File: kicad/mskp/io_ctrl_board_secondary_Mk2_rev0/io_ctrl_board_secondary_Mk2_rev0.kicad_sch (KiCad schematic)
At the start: 25 parts, among them J1 USB_C_I2C_input, J2 Keypad_matrix_connector_JST, J3 OLED_128x64, J4 I2C_aux_JST, J5 RJ45_SPI_I2C_input, J6 SPI_aux_JST, J7 I2C_aux_pads, U1 MCP23017_SP, U2 AMS1117

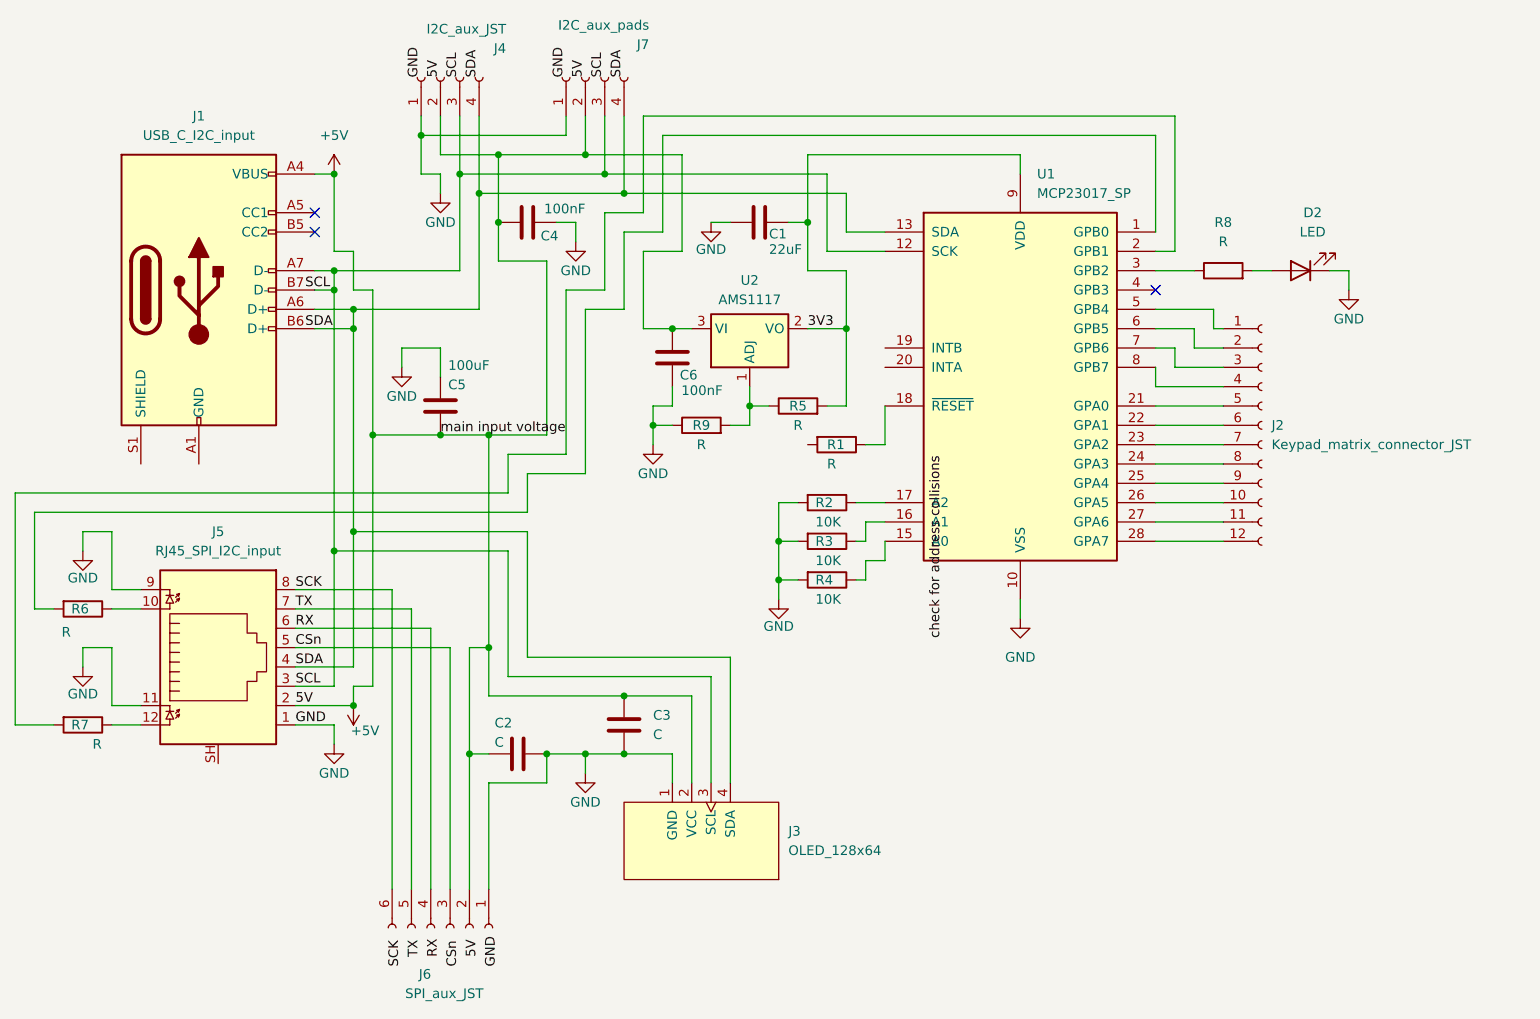
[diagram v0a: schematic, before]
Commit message: Further refinement of first drafts adding specific components
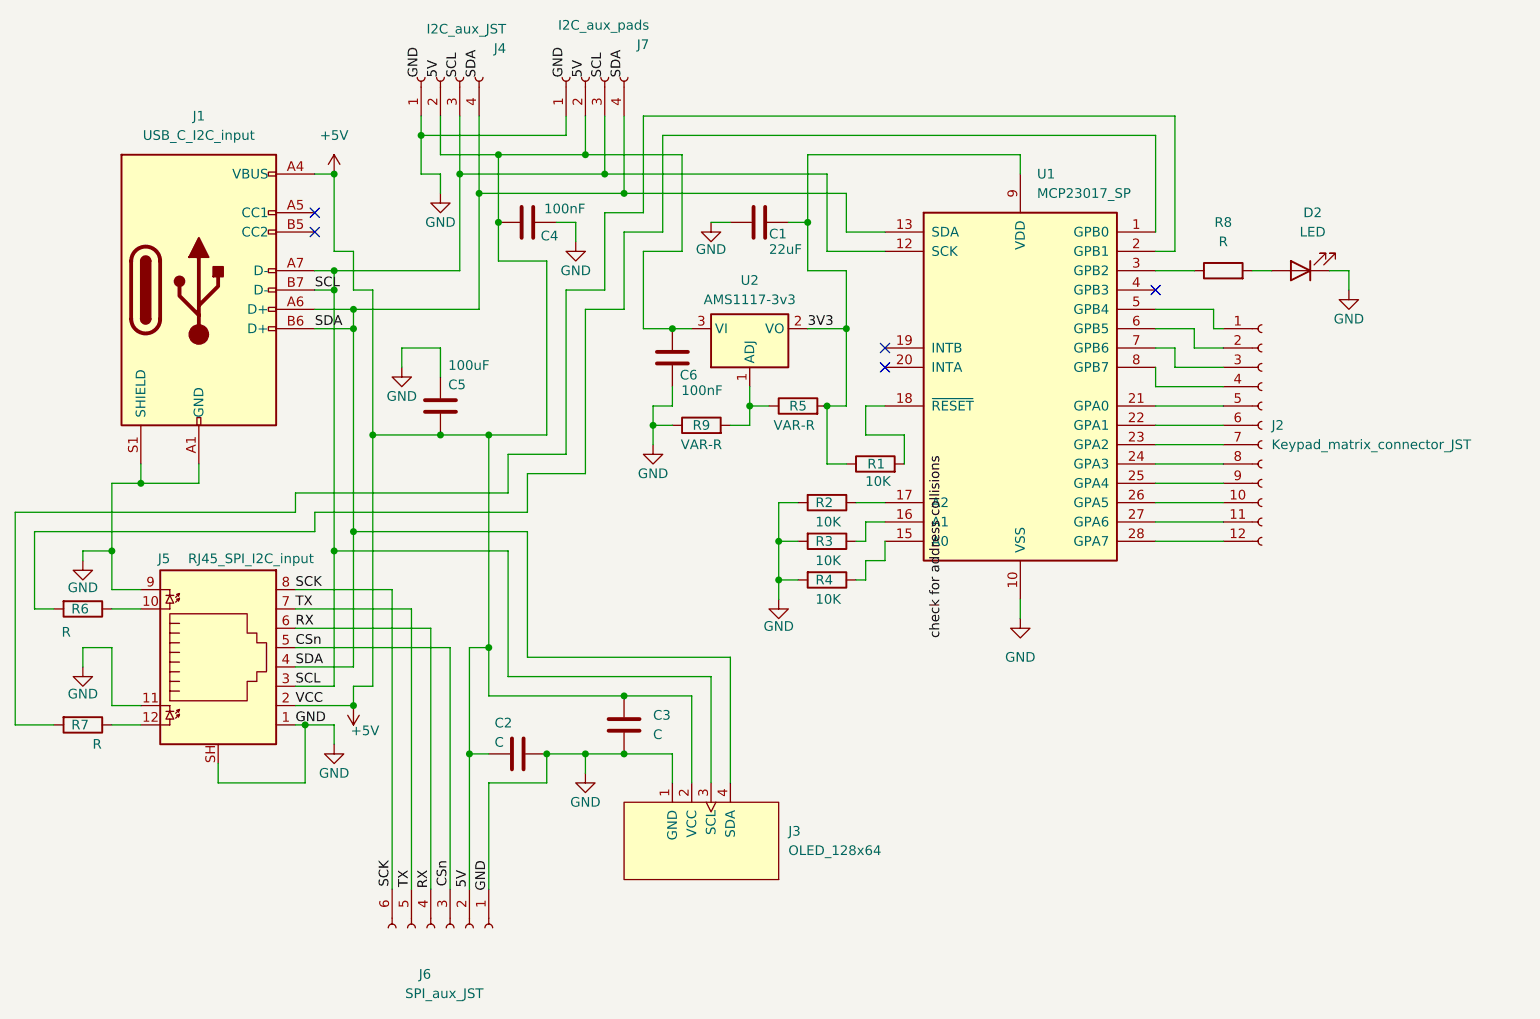
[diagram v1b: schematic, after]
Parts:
- R1: value R -> 10K
- R5, R9: value R -> VAR-R
- U2: value AMS1117 -> AMS1117-3v3
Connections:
- net 3V3: now also R1.1
- net GND: now also J1.A1 (GND), J1.A12 (GND), J1.B1 (GND), J1.B12 (GND), J1.S1 (SHIELD), J5.SH
- net at U1.18 (~{RESET}): now also R1.2; no longer R1.1
- no-connect marks 3 -> 5
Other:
- moved on the sheet: R1

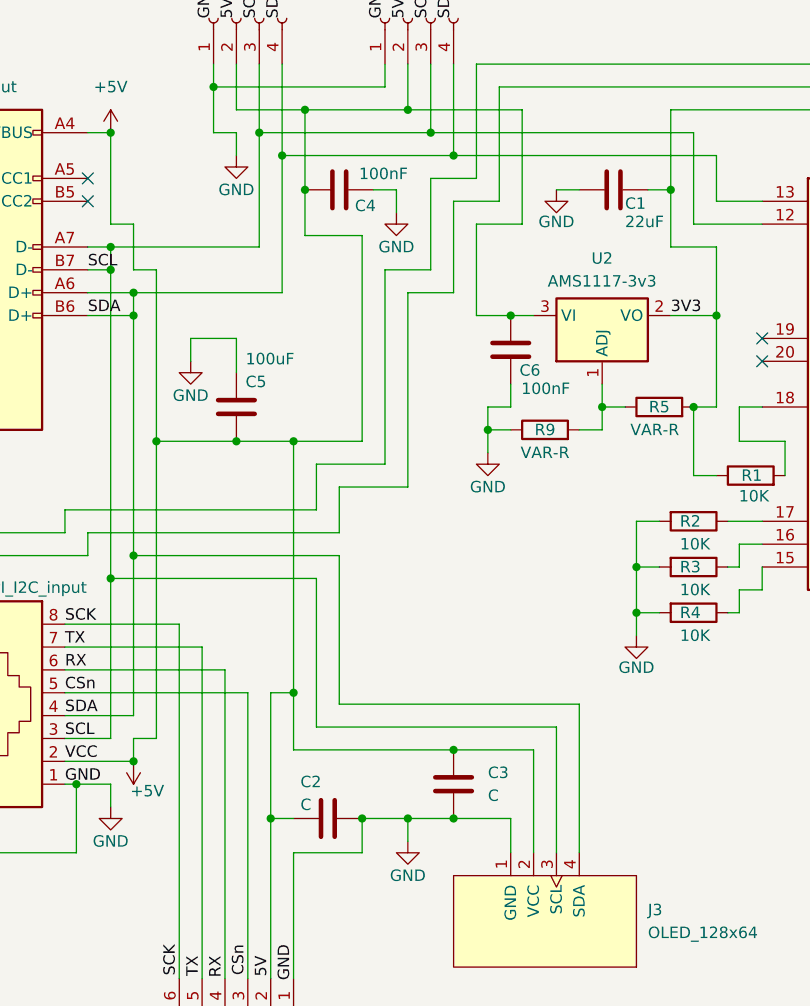
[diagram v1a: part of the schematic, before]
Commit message: Initital footprint assignment to all control boards
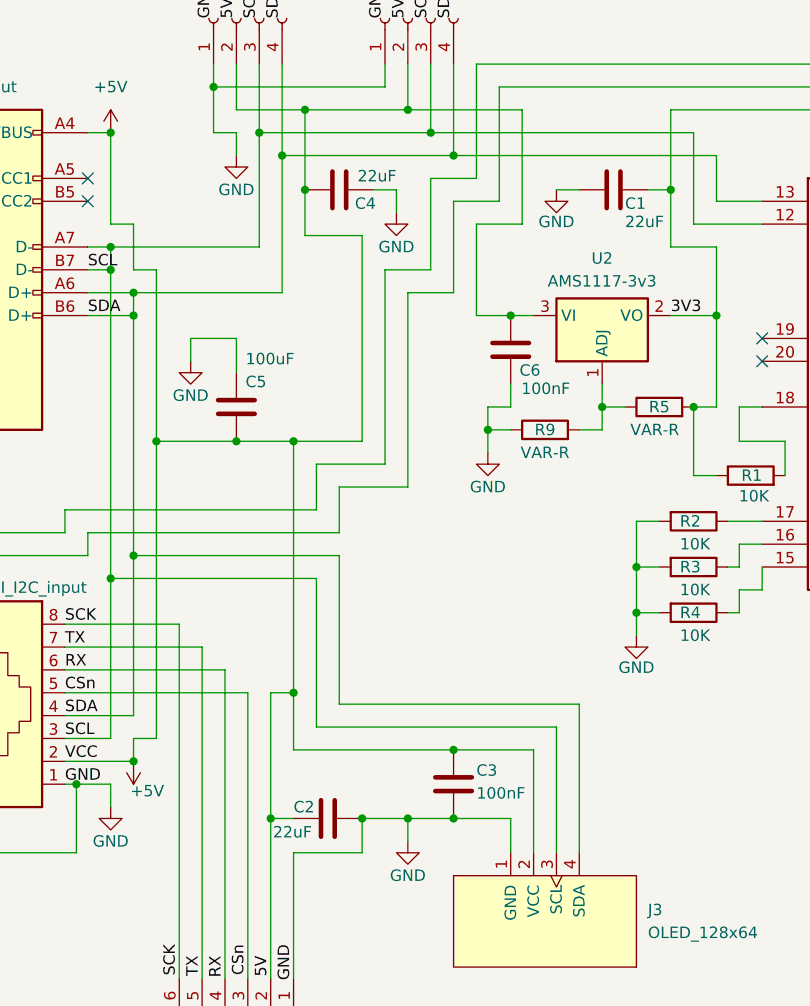
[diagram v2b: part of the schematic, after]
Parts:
- C1, C5, C6: footprint (none) -> Capacitor_SMD:C_1206_3216Metric_Pad1.33x1.80mm_HandSolder
- C2: value C -> 22uF; footprint (none) -> Capacitor_SMD:C_1206_3216Metric_Pad1.33x1.80mm_HandSolder
- C3: value C -> 100nF; footprint (none) -> Capacitor_SMD:C_1206_3216Metric_Pad1.33x1.80mm_HandSolder
- C4: value 100nF -> 22uF; footprint (none) -> Capacitor_SMD:C_1206_3216Metric_Pad1.33x1.80mm_HandSolder
- D2: footprint (none) -> LED_SMD:LED_0805_2012Metric_Pad1.15x1.40mm_HandSolder
- J1: footprint (none) -> Connector_USB:USB_C_Receptacle_GCT_USB4110
- J2: footprint (none) -> Connector_JST:JST_GH_SM12B-GHS-TB_1x12-1MP_P1.25mm_Horizontal
- J4: footprint (none) -> Connector_JST:JST_GH_SM04B-GHS-TB_1x04-1MP_P1.25mm_Horizontal
- J5: footprint (none) -> Connector_RJ:RJ45_Amphenol_RJHSE538X
- J6: footprint (none) -> Connector_JST:JST_GH_BM06B-GHS-TBT_1x06-1MP_P1.25mm_Vertical
- J7: footprint (none) -> Connector_PinSocket_2.54mm:PinSocket_1x04_P2.54mm_Vertical
- R1, R2, R3, R4, R5, R6, R7, R8, R9: footprint (none) -> Resistor_THT:R_Axial_DIN0207_L6.3mm_D2.5mm_P7.62mm_Horizontal
- U1: footprint Package_DIP:DIP-28_W7.62mm -> Package_DIP:DIP-28_W7.62mm_Socket
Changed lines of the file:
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@@
 			)
 		)
-		(property "Footprint" ""
+		(property "Footprint" "Connector_JST:JST_GH_BM06B-GHS-TBT_1x06-1MP_P1.25mm_Vertical"
 			(at 101.6 157.48 0)
 			(effects
@@
 			)
 		)
-		(property "Footprint" ""
+		(property "Footprint" "Capacitor_SMD:C_1206_3216Metric_Pad1.33x1.80mm_HandSolder"
 			(at 129.8448 78.74 0)
 			(effects
@@
 			)
 		)
-		(property "Footprint" ""
+		(property "Footprint" "Connector_RJ:RJ45_Amphenol_RJHSE538X"
 			(at 71.12 122.555 90)
 			(effects
@@
 			)
 		)
-		(property "Footprint" ""
+		(property "Footprint" "Connector_USB:USB_C_Receptacle_GCT_USB4110"
 			(at 72.39 73.66 0)
 			(effects
@@
 		(dnp no)
 		(property "Reference" "C2"
-			(at 107.442 130.556 90)
-			(effects
-				(font
-					(size 1.27 1.27)
-				)
-				(justify left)
-			)
-		)
-		(property "Value" "C"
-			(at 107.442 133.096 90)
-			(effects
-				(font
-					(size 1.27 1.27)
-				)
-				(justify left)
-			)
-		)
-		(property "Footprint" ""
+			(at 106.68 133.35 90)
+			(effects
+				(font
+					(size 1.27 1.27)
+				)
+				(justify left)
+			)
+		)
+		(property "Value" "22uF"
+			(at 104.394 136.144 90)
+			(effects
+				(font
+					(size 1.27 1.27)
+				)
+				(justify left)
+			)
+		)
+		(property "Footprint" "Capacitor_SMD:C_1206_3216Metric_Pad1.33x1.80mm_HandSolder"
 			(at 106.68 135.5852 0)
 			(effects
@@
 			)
 		)
-		(property "Footprint" ""
+		(property "Footprint" "Resistor_THT:R_Axial_DIN0207_L6.3mm_D2.5mm_P7.62mm_Horizontal"
 			(at 147.32 90.678 90)
 			(effects
@@
 			)
 		)
-		(property "Footprint" ""
+		(property "Footprint" "Connector_PinSocket_2.54mm:PinSocket_1x04_P2.54mm_Vertical"
 			(at 119.38 45.72 0)
 			(effects
@@
 			)
 		)
-		(property "Footprint" ""
+		(property "Footprint" "Capacitor_SMD:C_1206_3216Metric_Pad1.33x1.80mm_HandSolder"
 			(at 101.2952 85.09 0)
 			(effects
@@
 			)
 		)
-		(property "Footprint" ""
+		(property "Footprint" "Connector_JST:JST_GH_SM12B-GHS-TB_1x12-1MP_P1.25mm_Horizontal"
 			(at 208.28 91.44 0)
 			(effects
@@
 			)
 		)
-		(property "Footprint" ""
+		(property "Footprint" "Capacitor_SMD:C_1206_3216Metric_Pad1.33x1.80mm_HandSolder"
 			(at 138.43 65.7352 0)
 			(effects
@@
 			)
 		)
-		(property "Footprint" ""
+		(property "Footprint" "Resistor_THT:R_Axial_DIN0207_L6.3mm_D2.5mm_P7.62mm_Horizontal"
 			(at 53.34 113.792 90)
 			(effects
@@
 			)
 		)
-		(property "Footprint" ""
+		(property "Footprint" "Resistor_THT:R_Axial_DIN0207_L6.3mm_D2.5mm_P7.62mm_Horizontal"
 			(at 53.34 129.032 90)
 			(effects
@@
 			)
 		)
-		(property "Footprint" "Package_DIP:DIP-28_W7.62mm"
+		(property "Footprint" "Package_DIP:DIP-28_W7.62mm_Socket"
 			(at 181.61 111.76 0)
 			(effects
@@
 			)
 		)
-		(property "Footprint" ""
+		(property "Footprint" "Resistor_THT:R_Axial_DIN0207_L6.3mm_D2.5mm_P7.62mm_Horizontal"
 			(at 203.2 72.898 90)
 			(effects
@@
 			)
 		)
-		(property "Footprint" ""
+		(property "Footprint" "Resistor_THT:R_Axial_DIN0207_L6.3mm_D2.5mm_P7.62mm_Horizontal"
 			(at 151.13 99.822 90)
 			(effects
@@
 		(dnp no)
 		(property "Reference" "C4"
-			(at 115.824 66.548 90)
-			(effects
-				(font
-					(size 1.27 1.27)
-				)
-				(justify left)
-			)
-		)
-		(property "Value" "100nF"
-			(at 119.38 62.992 90)
-			(effects
-				(font
-					(size 1.27 1.27)
-				)
-				(justify left)
-			)
-		)
-		(property "Footprint" ""
+			(at 115.824 66.294 90)
+			(effects
+				(font
+					(size 1.27 1.27)
+				)
+				(justify left)
+			)
+		)
+		(property "Value" "22uF"
+			(at 118.11 63.246 90)
+			(effects
+				(font
+					(size 1.27 1.27)
+				)
+				(justify left)
+			)
+		)
+		(property "Footprint" "Capacitor_SMD:C_1206_3216Metric_Pad1.33x1.80mm_HandSolder"
 			(at 115.57 63.8048 0)
 			(effects
@@
 			)
 		)
-		(property "Footprint" ""
+		(property "Footprint" "LED_SMD:LED_0805_2012Metric_Pad1.15x1.40mm_HandSolder"
 			(at 213.36 71.12 0)
 			(effects
@@
 			)
 		)
-		(property "Footprint" ""
+		(property "Footprint" "Connector_JST:JST_GH_SM04B-GHS-TB_1x04-1MP_P1.25mm_Horizontal"
 			(at 100.33 45.72 0)
 			(effects
@@
 			)
 		)
-		(property "Footprint" ""
+		(property "Footprint" "Resistor_THT:R_Axial_DIN0207_L6.3mm_D2.5mm_P7.62mm_Horizontal"
 			(at 151.13 104.902 90)
 			(effects
@@
 		(on_board yes)
 		(dnp no)
-		(fields_autoplaced yes)
 		(property "Reference" "C3"
-			(at 128.27 129.5399 0)
-			(effects
-				(font
-					(size 1.27 1.27)
-				)
-				(justify left)
-			)
-		)
-		(property "Value" "C"
-			(at 128.27 132.0799 0)
-			(effects
-				(font
-					(size 1.27 1.27)
-				)
-				(justify left)
-			)
-		)
-		(property "Footprint" ""
+			(at 127 129.286 0)
+			(effects
+				(font
+					(size 1.27 1.27)
+				)
+				(justify left)
+			)
+		)
+		(property "Value" "100nF"
+			(at 127 131.826 0)
+			(effects
+				(font
+					(size 1.27 1.27)
+				)
+				(justify left)
+			)
+		)
+		(property "Footprint" "Capacitor_SMD:C_1206_3216Metric_Pad1.33x1.80mm_HandSolder"
 			(at 125.4252 134.62 0)
 			(effects
@@
 			)
 		)
-		(property "Footprint" ""
+		(property "Footprint" "Resistor_THT:R_Axial_DIN0207_L6.3mm_D2.5mm_P7.62mm_Horizontal"
 			(at 134.62 93.218 90)
 			(effects
@@
 			)
 		)
-		(property "Footprint" ""
+		(property "Footprint" "Resistor_THT:R_Axial_DIN0207_L6.3mm_D2.5mm_P7.62mm_Horizontal"
 			(at 151.13 109.982 90)
 			(effects
@@
 			)
 		)
-		(property "Footprint" ""
+		(property "Footprint" "Resistor_THT:R_Axial_DIN0207_L6.3mm_D2.5mm_P7.62mm_Horizontal"
 			(at 157.48 98.298 90)
 			(effects

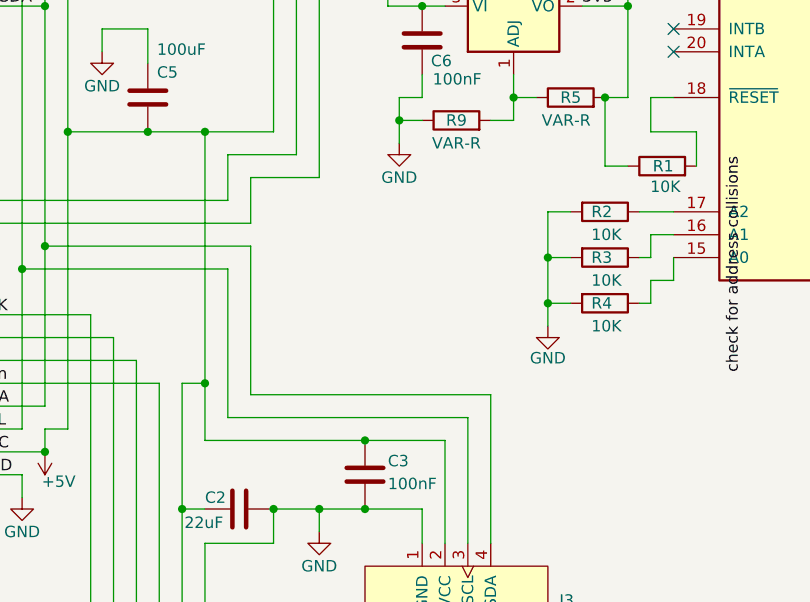
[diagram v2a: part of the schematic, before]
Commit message: Initial layout of PCB traces on io_ctrl_board_secondary_Mk2_rev0
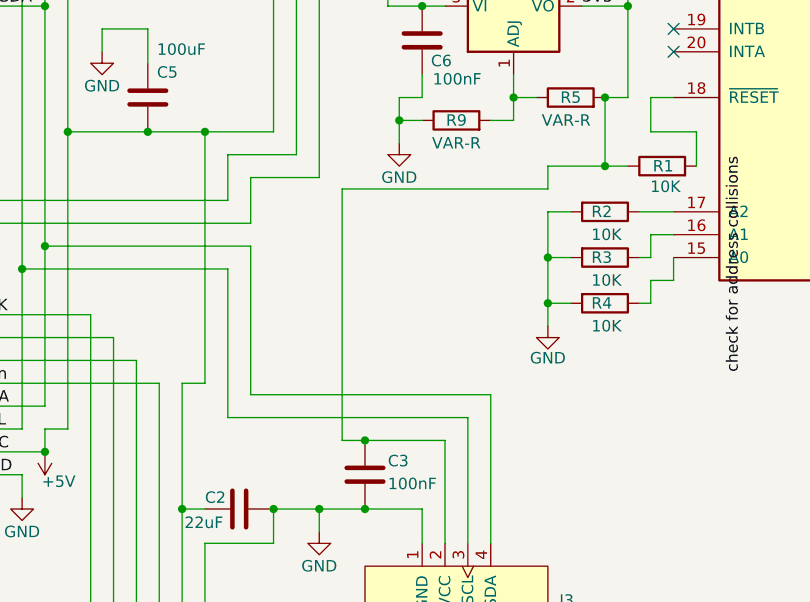
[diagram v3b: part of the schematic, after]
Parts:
- J6: footprint Connector_JST:JST_GH_BM06B-GHS-TBT_1x06-1MP_P1.25mm_Vertical -> Connector_JST:JST_GH_SM06B-GHS-TB_1x06-1MP_P1.25mm_Horizontal
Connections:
- net +5V: no longer C3.1, J3.2 (VCC)
- net 3V3: now also C3.1, J3.2 (VCC)
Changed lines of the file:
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@@
+	)
+	(junction
+		(at 151.13 96.52)
+		(diameter 0)
+		(color 0 0 0 0)
 	)
 	(junction
@@
 	)
 	(junction
+		(at 86.36 107.95)
+		(diameter 0)
+		(color 0 0 0 0)
+	)
+	(junction
+		(at 86.36 71.12)
+		(diameter 0)
+		(color 0 0 0 0)
+	)
+	(junction
+		(at 121.92 58.42)
+		(diameter 0)
+		(color 0 0 0 0)
+	)
+	(junction
+		(at 119.38 55.88)
+		(diameter 0)
+		(color 0 0 0 0)
+	)
+	(junction
+		(at 105.41 60.96)
+		(diameter 0)
+		(color 0 0 0 0)
+	)
+	(junction
+		(at 60.96 99.06)
+		(diameter 0)
+		(color 0 0 0 0)
+	)
+	(junction
+		(at 82.55 130.81)
+		(diameter 0)
+		(color 0 0 0 0)
+	)
+	(junction
+		(at 57.15 107.95)
+		(diameter 0)
+		(color 0 0 0 0)
+	)
+	(junction
+		(at 119.38 134.62)
+		(diameter 0)
+		(color 0 0 0 0)
+	)
+	(junction
+		(at 130.81 78.74)
+		(diameter 0)
+		(color 0 0 0 0)
+	)
+	(junction
+		(at 107.95 64.77)
+		(diameter 0)
+		(color 0 0 0 0)
+	)
+	(junction
 		(at 124.46 127)
-		(diameter 0)
-		(color 0 0 0 0)
-	)
-	(junction
-		(at 86.36 107.95)
-		(diameter 0)
-		(color 0 0 0 0)
-	)
-	(junction
-		(at 86.36 71.12)
-		(diameter 0)
-		(color 0 0 0 0)
-	)
-	(junction
-		(at 121.92 58.42)
-		(diameter 0)
-		(color 0 0 0 0)
-	)
-	(junction
-		(at 106.68 120.65)
-		(diameter 0)
-		(color 0 0 0 0)
-	)
-	(junction
-		(at 119.38 55.88)
-		(diameter 0)
-		(color 0 0 0 0)
-	)
-	(junction
-		(at 105.41 60.96)
-		(diameter 0)
-		(color 0 0 0 0)
-	)
-	(junction
-		(at 60.96 99.06)
-		(diameter 0)
-		(color 0 0 0 0)
-	)
-	(junction
-		(at 82.55 130.81)
-		(diameter 0)
-		(color 0 0 0 0)
-	)
-	(junction
-		(at 57.15 107.95)
-		(diameter 0)
-		(color 0 0 0 0)
-	)
-	(junction
-		(at 119.38 134.62)
-		(diameter 0)
-		(color 0 0 0 0)
-	)
-	(junction
-		(at 130.81 78.74)
-		(diameter 0)
-		(color 0 0 0 0)
-	)
-	(junction
-		(at 107.95 64.77)
 		(diameter 0)
 		(color 0 0 0 0)
@@
 	(wire
 		(pts
+			(xy 124.46 127) (xy 121.92 127)
+		)
+		(stroke
+			(width 0)
+			(type default)
+		)
+	)
+	(wire
+		(pts
 			(xy 138.43 121.92) (xy 138.43 138.43)
 		)
@@
 	(wire
 		(pts
+			(xy 121.92 99.06) (xy 144.78 99.06)
+		)
+		(stroke
+			(width 0)
+			(type default)
+		)
+	)
+	(wire
+		(pts
 			(xy 144.78 111.76) (xy 147.32 111.76)
 		)
@@
 	(wire
 		(pts
-			(xy 106.68 127) (xy 124.46 127)
-		)
-		(stroke
-			(width 0)
-			(type default)
-		)
-	)
-	(wire
-		(pts
 			(xy 118.11 64.77) (xy 118.11 67.31)
 		)
@@
 	(wire
 		(pts
+			(xy 121.92 127) (xy 121.92 99.06)
+		)
+		(stroke
+			(width 0)
+			(type default)
+		)
+	)
+	(wire
+		(pts
 			(xy 109.22 107.95) (xy 86.36 107.95)
 		)
@@
 	(wire
 		(pts
+			(xy 144.78 96.52) (xy 151.13 96.52)
+		)
+		(stroke
+			(width 0)
+			(type default)
+		)
+	)
+	(wire
+		(pts
 			(xy 97.79 50.8) (xy 97.79 53.34)
 		)
@@
 	(wire
 		(pts
+			(xy 144.78 99.06) (xy 144.78 96.52)
+		)
+		(stroke
+			(width 0)
+			(type default)
+		)
+	)
+	(wire
+		(pts
 			(xy 86.36 107.95) (xy 86.36 125.73)
 		)
@@
 		(pts
 			(xy 91.44 92.71) (xy 91.44 125.73)
-		)
-		(stroke
-			(width 0)
-			(type default)
-		)
-	)
-	(wire
-		(pts
-			(xy 106.68 120.65) (xy 106.68 127)
 		)
 		(stroke
@@
 			)
 		)
-		(property "Footprint" "Connector_JST:JST_GH_BM06B-GHS-TBT_1x06-1MP_P1.25mm_Vertical"
+		(property "Footprint" "Connector_JST:JST_GH_SM06B-GHS-TB_1x06-1MP_P1.25mm_Horizontal"
 			(at 101.6 157.48 0)
 			(effects
